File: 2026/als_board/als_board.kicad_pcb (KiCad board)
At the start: 2 copper layers, 60 x 8 mm, 18 parts, among them J1 MAIN, J2 i2c, J3 PROG, U1 GM7333, U2 ME6209A50M3G, U3 CH32V003JxMx, U4 MAX485E

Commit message: ALS finishing touches
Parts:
- added G***: LOGO, MAGLab_Logo:MAGLab_Website_Small, F.Cu at (128.5, 105.0)
- added G***: LOGO, MAGLab_Logo:MAGLab_Symbol_Fine, B.Cu at (137.7, 103.6)
- added R4: 5k1, Resistor_SMD:R_0603_1608Metric, F.Cu at (111.8, 103.5)
- added R5: 5k1, Resistor_SMD:R_0603_1608Metric, F.Cu at (111.0, 105.8)
- added R6: 10k, Resistor_SMD:R_0603_1608Metric, F.Cu at (147.8, 107.0)
- added R7: 10k, Resistor_SMD:R_0603_1608Metric, F.Cu at (149.2, 107.0)
- moved R3 1.68 mm to (112.5, 105.8)
- moved R2 1.50 mm to (122.5, 105.5)
- moved U4 1.50 mm to (117.0, 105.5)
- moved C1 0.25 mm to (109.0, 104.8)
- moved C6 0.25 mm to (111.8, 102.0)
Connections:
- net Net-(J2-Pin_2) renamed /SCL
- net Net-(J2-Pin_3) renamed /SDA
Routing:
- net +5V: track 12.9 -> 18.5 mm, vias 1 -> 3
- net GND: track 65.8 -> 69.7 mm, vias 2 -> 17
- net /12V_FIL: track 20.7 -> 23.4 mm
- net Net-(J1-Pin_2): track 6.80 -> 9.10 mm
- net +3V3: track 32.1 -> 34.2 mm, vias 1 -> 8
- net Net-(J1-Pin_3): track 13.2 -> 14.7 mm
- net Net-(U3-PD6/PA1): track 20.5 -> 19.5 mm
- net Net-(U3-PA2): track 21.6 -> 20.7 mm
- net +12V: track 10.0 -> 10.7 mm, vias 1 -> 5
- added copper zone on B.Cu, net +12V
- added copper zone on F.Cu, net +12V
- added copper zone on B.Cu, net +3V3
- added copper zone on F.Cu, net +3V3
- added copper zone on B.Cu, net +5V
- added copper zone on F.Cu, net +5V
- added copper zone on B.Cu, net /12V_FIL
- added copper zone on B.Cu, net GND
- added copper zone on F.Cu, net GND
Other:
- board text added: "${TITLE}"
- board text added: "Rev. ${REVISION}"

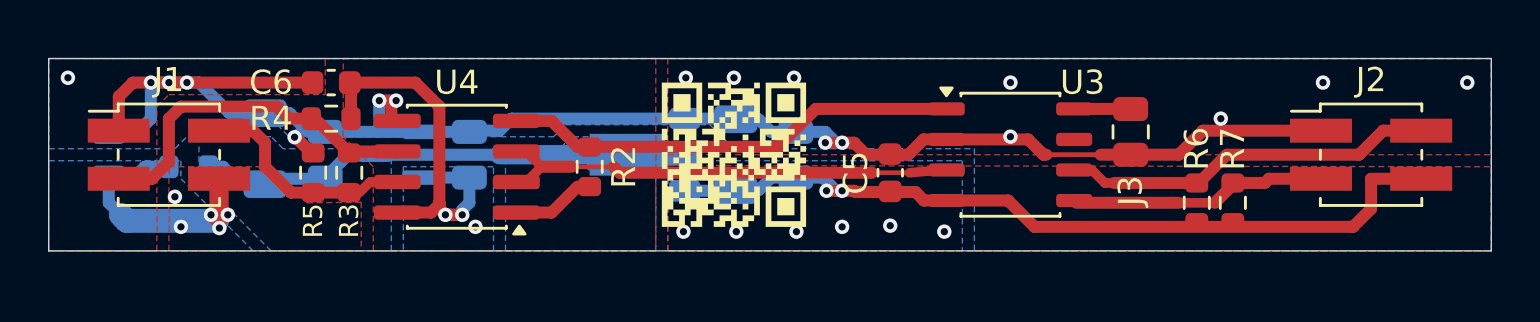
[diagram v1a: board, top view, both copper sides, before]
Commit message: ALS board with startup resistors for direction and output biasing (output off, high by default)
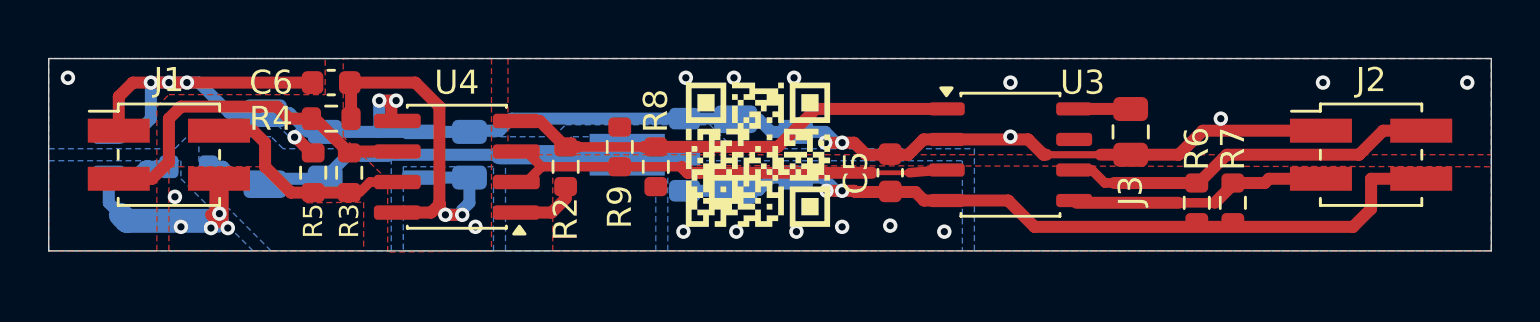
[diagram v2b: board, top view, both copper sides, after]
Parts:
- added R8: 1.5M, Resistor_SMD:R_0603_1608Metric, F.Cu at (125.2, 105.5)
- added R9: 1.5M, Resistor_SMD:R_0603_1608Metric, F.Cu at (123.8, 104.7)
- moved G*** 3.00 mm to (137.7, 106.6)
- moved G*** 1.00 mm to (129.5, 105.0)
- moved R2 1.00 mm to (121.5, 105.5)
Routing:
- net Net-(U3-PD6/PA1): track 19.5 -> 20.0 mm

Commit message: Ambient light sensor modification for better layout with better pad configuration and soldermasking
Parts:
- added J4: Conn_01x02, Resistor_SMD:R_0805_2012Metric, B.Cu at (151.5, 105.0)
- J1: footprint Connector_PinHeader_2.00mm:PinHeader_2x02_P2.00mm_Vertical_SMD -> this:PADS_4
- J2: value i2c -> Conn_01x02; footprint Connector_PinHeader_2.00mm:PinHeader_2x02_P2.00mm_Vertical_SMD -> Resistor_SMD:R_1206_3216Metric
- moved J1 3.00 mm to (102.0, 105.0), turned to -90 degrees
- moved J2 1.30 mm to (153.8, 105.5), turned to -90 degrees
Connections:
- J2 pad 2: /SCL -> +3V3
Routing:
- net /SCL: track 15.6 -> 9.94 mm, vias 0 -> 1
- net Net-(J1-Pin_2): track 9.10 -> 14.2 mm, vias 0 -> 2
- net +3V3: track 34.2 -> 29.8 mm
- net GND: track 69.7 -> 65.3 mm, vias 17 -> 16
- net +12V: track 10.7 -> 12.6 mm
- net /SDA: track 10.7 -> 9.34 mm, vias 0 -> 1
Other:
- board size 60 x 8 mm -> 55 x 8 mm
